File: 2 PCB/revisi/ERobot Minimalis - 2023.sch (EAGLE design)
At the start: 12 parts, among them J1 215297-6, J2 215297-6, J3 1935161, J4 215297-6, U1 STMICROELECTRONICS_L7805CVSTM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, U2 STMICROELECTRONICS_L7805CVSTM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

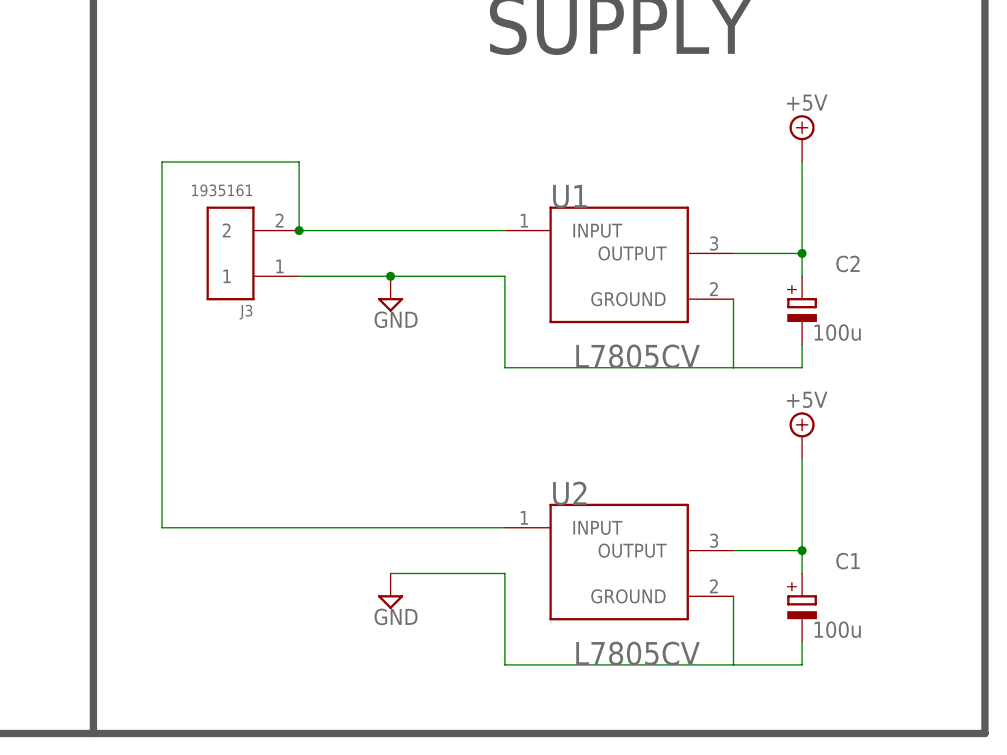
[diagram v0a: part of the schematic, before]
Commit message: tambah 1 baterai PCB
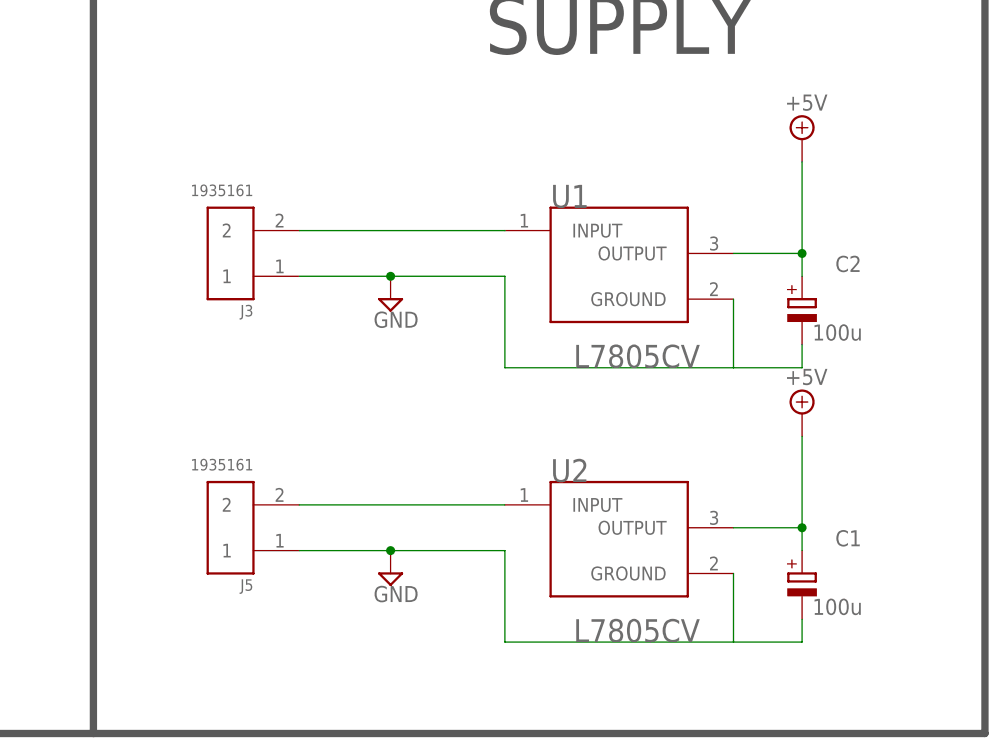
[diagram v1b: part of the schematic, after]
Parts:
- added J5: 1935161, 1935161:1935161
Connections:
- new net N$2: J3.2, U1.INPUT
- net GND: now also J5.1
- net N$1: now also J5.2; no longer J3.2, U1.INPUT
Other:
- moved on the sheet: C1, U2
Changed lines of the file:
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@@
 <part name="U2" library="STMicroelectronics - L7805CV" deviceset="STMICROELECTRONICS_L7805CV" device="STMICROELECTRONICS_L7805CV_0_0"/>
 <part name="SUPPLY13" library="supply2" library_urn="urn:adsk.eagle:library:372" deviceset="GND" device=""/>
+<part name="J5" library="1935161" deviceset="1935161" device=""/>
 </parts>
 <sheets>
@@
 <attribute name="VALUE" x="220.345" y="271.145" size="1.778" layer="96" rot="R180"/>
 </instance>
-<instance part="C1" gate="G$1" x="322.58" y="167.64" smashed="yes">
-<attribute name="NAME" x="326.263" y="170.6626" size="1.778" layer="95"/>
-<attribute name="VALUE" x="323.723" y="163.0426" size="1.778" layer="96"/>
-</instance>
-<instance part="SUPPLY12" gate="+5V" x="322.58" y="185.42" smashed="yes">
-<attribute name="VALUE" x="320.675" y="188.595" size="1.778" layer="96"/>
-</instance>
-<instance part="U2" gate="G$0" x="292.1" y="182.88" smashed="yes">
-<attribute name="NAME" x="294.64" y="180.34" size="2.54" layer="95" align="top-left"/>
-</instance>
-<instance part="SUPPLY13" gate="GND" x="276.86" y="167.64" smashed="yes">
-<attribute name="VALUE" x="274.955" y="164.465" size="1.778" layer="96"/>
+<instance part="C1" gate="G$1" x="322.58" y="170.18" smashed="yes">
+<attribute name="NAME" x="326.263" y="173.2026" size="1.778" layer="95"/>
+<attribute name="VALUE" x="323.723" y="165.5826" size="1.778" layer="96"/>
+</instance>
+<instance part="SUPPLY12" gate="+5V" x="322.58" y="187.96" smashed="yes">
+<attribute name="VALUE" x="320.675" y="191.135" size="1.778" layer="96"/>
+</instance>
+<instance part="U2" gate="G$0" x="292.1" y="185.42" smashed="yes">
+<attribute name="NAME" x="294.64" y="182.88" size="2.54" layer="95" align="top-left"/>
+</instance>
+<instance part="SUPPLY13" gate="GND" x="276.86" y="170.18" smashed="yes">
+<attribute name="VALUE" x="274.955" y="167.005" size="1.778" layer="96"/>
+</instance>
+<instance part="J5" gate="G$1" x="259.08" y="175.26" smashed="yes" rot="R180">
+<attribute name="NAME" x="261.62548125" y="169.532659375" size="1.272740625" layer="95" rot="R180"/>
+<attribute name="VALUE" x="261.62808125" y="182.90423125" size="1.274040625" layer="96" rot="R180"/>
 </instance>
 </instances>
@@
 </segment>
 <segment>
+<pinref part="C1" gate="G$1" pin="-"/>
+<wire x1="322.58" y1="165.1" x2="322.58" y2="162.56" width="0.1524" layer="91"/>
+<wire x1="322.58" y1="162.56" x2="314.96" y2="162.56" width="0.1524" layer="91"/>
+<pinref part="U2" gate="G$0" pin="GROUND"/>
+<wire x1="289.56" y1="162.56" x2="314.96" y2="162.56" width="0.1524" layer="91"/>
+<wire x1="314.96" y1="162.56" x2="314.96" y2="170.18" width="0.1524" layer="91"/>
+<wire x1="289.56" y1="172.72" x2="289.56" y2="162.56" width="0.1524" layer="91"/>
 <pinref part="SUPPLY13" gate="GND" pin="GND"/>
-<wire x1="276.86" y1="170.18" x2="289.56" y2="170.18" width="0.1524" layer="91"/>
-<pinref part="C1" gate="G$1" pin="-"/>
-<wire x1="322.58" y1="162.56" x2="322.58" y2="160.02" width="0.1524" layer="91"/>
-<wire x1="322.58" y1="160.02" x2="314.96" y2="160.02" width="0.1524" layer="91"/>
-<pinref part="U2" gate="G$0" pin="GROUND"/>
-<wire x1="289.56" y1="160.02" x2="314.96" y2="160.02" width="0.1524" layer="91"/>
-<wire x1="314.96" y1="160.02" x2="314.96" y2="167.64" width="0.1524" layer="91"/>
-<wire x1="289.56" y1="170.18" x2="289.56" y2="160.02" width="0.1524" layer="91"/>
+<wire x1="276.86" y1="172.72" x2="289.56" y2="172.72" width="0.1524" layer="91"/>
+<pinref part="J5" gate="G$1" pin="1"/>
+<wire x1="266.7" y1="172.72" x2="276.86" y2="172.72" width="0.1524" layer="91"/>
+<junction x="276.86" y="172.72"/>
 </segment>
 </net>
@@
 <pinref part="C1" gate="G$1" pin="+"/>
 <pinref part="SUPPLY12" gate="+5V" pin="+5V"/>
-<wire x1="322.58" y1="182.88" x2="322.58" y2="172.72" width="0.1524" layer="91"/>
+<wire x1="322.58" y1="185.42" x2="322.58" y2="175.26" width="0.1524" layer="91"/>
 <pinref part="U2" gate="G$0" pin="OUTPUT"/>
-<wire x1="322.58" y1="172.72" x2="322.58" y2="170.18" width="0.1524" layer="91"/>
-<wire x1="314.96" y1="172.72" x2="322.58" y2="172.72" width="0.1524" layer="91"/>
-<junction x="322.58" y="172.72"/>
+<wire x1="322.58" y1="175.26" x2="322.58" y2="172.72" width="0.1524" layer="91"/>
+<wire x1="314.96" y1="175.26" x2="322.58" y2="175.26" width="0.1524" layer="91"/>
+<junction x="322.58" y="175.26"/>
 </segment>
 </net>
@@
 </segment>
 </net>
+<net name="N$2" class="0">
+<segment>
+<pinref part="U1" gate="G$0" pin="INPUT"/>
+<pinref part="J3" gate="G$1" pin="2"/>
+<wire x1="266.7" y1="208.28" x2="289.56" y2="208.28" width="0.1524" layer="91"/>
+</segment>
+</net>
 <net name="N$1" class="0">
 <segment>
-<pinref part="J3" gate="G$1" pin="2"/>
-<pinref part="U1" gate="G$0" pin="INPUT"/>
-<wire x1="266.7" y1="208.28" x2="289.56" y2="208.28" width="0.1524" layer="91"/>
-<wire x1="266.7" y1="208.28" x2="266.7" y2="215.9" width="0.1524" layer="91"/>
-<junction x="266.7" y="208.28"/>
-<wire x1="266.7" y1="215.9" x2="251.46" y2="215.9" width="0.1524" layer="91"/>
+<pinref part="J5" gate="G$1" pin="2"/>
 <pinref part="U2" gate="G$0" pin="INPUT"/>
-<wire x1="251.46" y1="215.9" x2="251.46" y2="175.26" width="0.1524" layer="91"/>
-<wire x1="251.46" y1="175.26" x2="289.56" y2="175.26" width="0.1524" layer="91"/>
-</segment>
-</net>
+<wire x1="266.7" y1="177.8" x2="289.56" y2="177.8" width="0.1524" layer="91"/>
+</segment>
+</net>
